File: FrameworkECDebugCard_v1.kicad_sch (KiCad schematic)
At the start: 25 parts, among them J1 Conn_01x05, P1 USB_C_Plug_USB2.0, P2 USB_B_Micro, U1 FT230XS

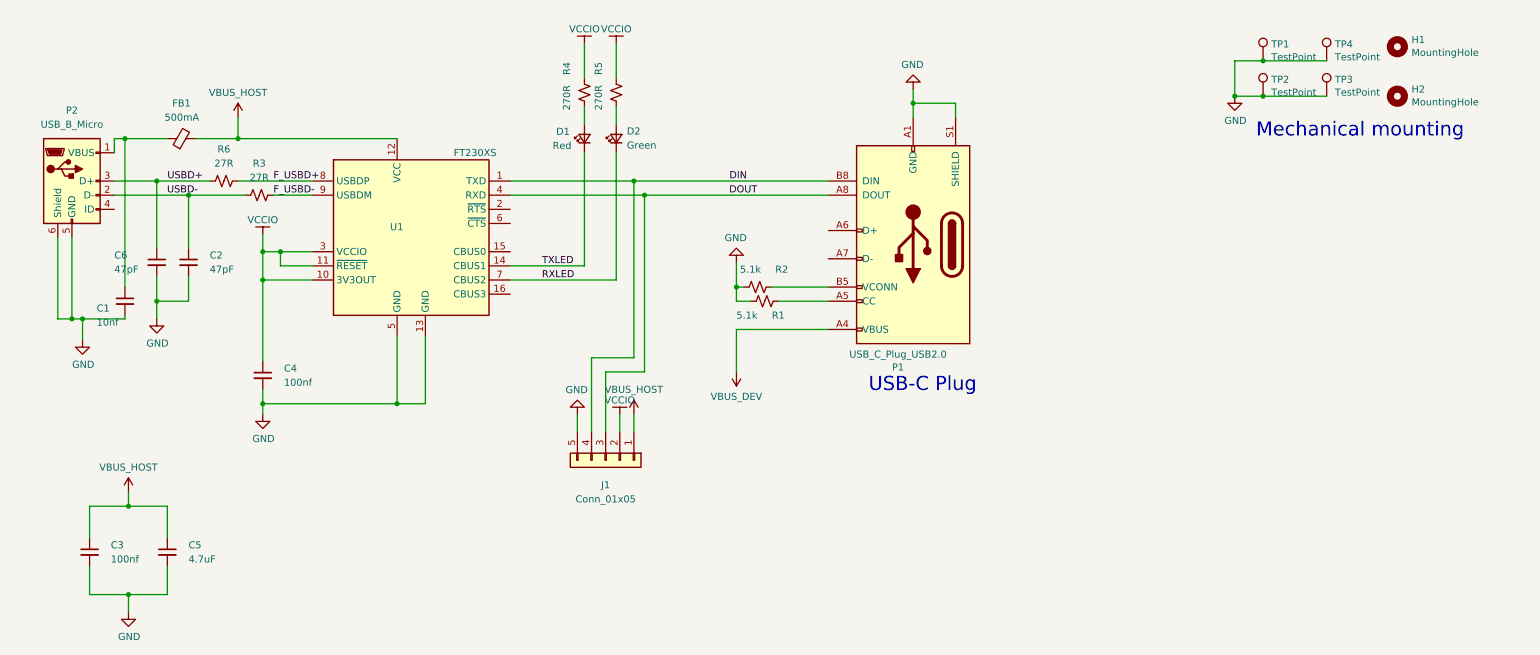
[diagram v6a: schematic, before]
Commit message: ec card 3: recessed mid-mount usb c receptacle, fully rerouted
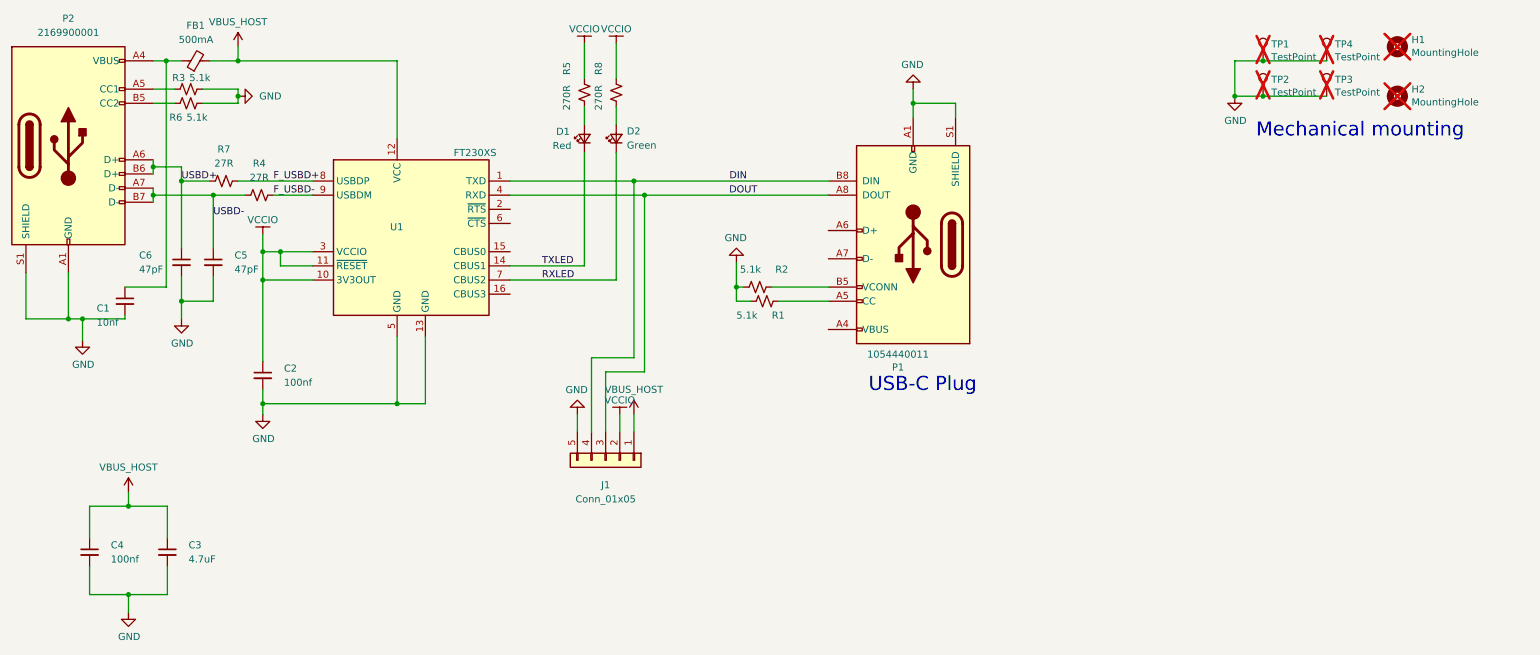
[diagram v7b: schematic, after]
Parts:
- added R3, R6: 5.1k, Resistor_SMD:R_0402_1005Metric, symbol Device:R_Small_US
- H1, H2, TP1, TP2, TP3, TP4: now not fitted
- P1: value USB_C_Plug_USB2.0 -> 1054440011; footprint FrameworkECDebugCard_v1:USB_C_Plug_Molex_105444 -> FrameworkECDebugCard_v1:USB_C_Plug_Molex_105444_SmallPads
- P2: value USB_B_Micro -> 2169900001; footprint Connector_USB:USB_Micro-B_Amphenol_10104110_Horizontal -> FrameworkECDebugCard_v1:USB4510-03-1-A_GCT; symbol Connector:USB_B_Micro -> Connector:USB_C_Receptacle_USB2.0_14P
- renumbered C4 to C2, C5 to C3, C3 to C4, C2 to C5, R3 to R4, R4 to R5, R6 to R7, R5 to R8
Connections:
- net GND: now also P2.A1 (GND), P2.A12 (GND), P2.B1 (GND), P2.B12 (GND), P2.S1 (SHIELD), R3.1, R6.1; no longer P2.5 (GND), P2.6 (Shield)
- net USBD+: now also P2.A6 (D+), P2.B6 (D+); no longer P2.3 (D+)
- net USBD-: now also P2.A7 (D-), P2.B7 (D-); no longer P2.2 (D-)
- net at C1.1, FB1.1: now also P2.A4 (VBUS), P2.A9 (VBUS), P2.B4 (VBUS), P2.B9 (VBUS); no longer P2.1 (VBUS)
- net VBUS_DEV: no longer names the net of P1.A4 (VBUS), P1.A9 (VBUS), P1.B4 (VBUS), P1.B9 (VBUS)
- new net: P2.B5 (CC2), R6.2
- new net: P2.A5 (CC1), R3.2
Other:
- moved on the sheet: C5, C6, FB1

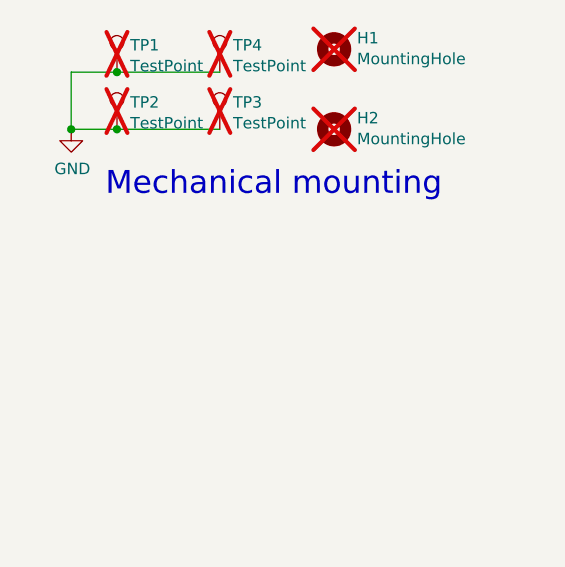
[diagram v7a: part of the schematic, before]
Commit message: ec3: rebuild the pcb to the same shape as the usb c card; not routed
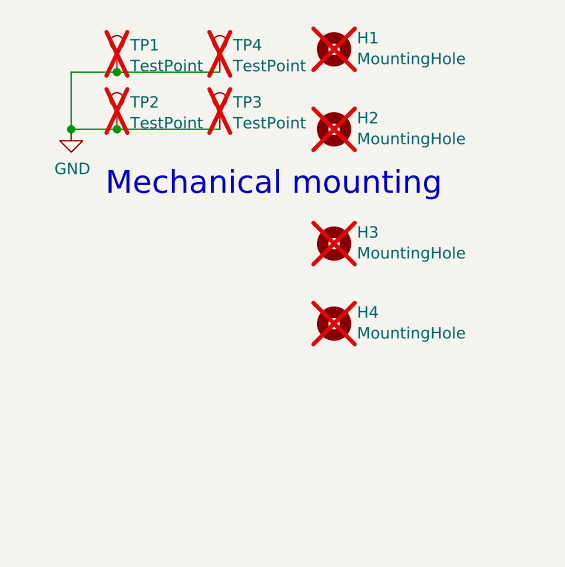
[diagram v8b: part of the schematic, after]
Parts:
- added H3, H4: MountingHole, FrameworkECDebugCard_v1:MountingHole_1.5mm_NPTH, symbol Mechanical:MountingHole
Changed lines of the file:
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@@
+	)
+	(symbol
+		(lib_id "Mechanical:MountingHole")
+		(at 262.89 41.91 0)
+		(unit 1)
+		(exclude_from_sim no)
+		(in_bom yes)
+		(on_board yes)
+		(dnp yes)
+		(property "Reference" "H3"
+			(at 265.43 40.6654 0)
+			(effects
+				(font
+					(size 1.27 1.27)
+				)
+				(justify left)
+			)
+		)
+		(property "Value" "MountingHole"
+			(at 265.43 42.9768 0)
+			(effects
+				(font
+					(size 1.27 1.27)
+				)
+				(justify left)
+			)
+		)
+		(property "Footprint" "FrameworkECDebugCard_v1:MountingHole_1.5mm_NPTH"
+			(at 262.89 41.91 0)
+			(effects
+				(font
+					(size 1.27 1.27)
+				)
+				(hide yes)
+			)
+		)
+		(property "Datasheet" "~"
+			(at 262.89 41.91 0)
+			(effects
+				(font
+					(size 1.27 1.27)
+				)
+				(hide yes)
+			)
+		)
+		(property "Description" ""
+			(at 262.89 41.91 0)
+			(effects
+				(font
+					(size 1.27 1.27)
+				)
+				(hide yes)
+			)
+		)
+		(instances
+			(project "FrameworkECDebugCard_v1"
+				(path "/6d9454a9-630b-4948-a74b-a7b030d302e8"
+					(reference "H3")
+					(unit 1)
+				)
+			)
+		)
 	)
 	(symbol
@@
 					(unit 1)
 				)
+			)
+		)
+	)
+	(symbol
+		(lib_id "Mechanical:MountingHole")
+		(at 262.89 50.8 0)
+		(unit 1)
+		(exclude_from_sim no)
+		(in_bom yes)
+		(on_board yes)
+		(dnp yes)
+		(property "Reference" "H4"
+			(at 265.43 49.5554 0)
+			(effects
+				(font
+					(size 1.27 1.27)
+				)
+				(justify left)
+			)
+		)
+		(property "Value" "MountingHole"
+			(at 265.43 51.8668 0)
+			(effects
+				(font
+					(size 1.27 1.27)
+				)
+				(justify left)
+			)
+		)
+		(property "Footprint" "FrameworkECDebugCard_v1:MountingHole_1.5mm_NPTH"
+			(at 262.89 50.8 0)
+			(effects
+				(font
+					(size 1.27 1.27)
+				)
+				(hide yes)
+			)
+		)
+		(property "Datasheet" "~"
+			(at 262.89 50.8 0)
+			(effects
+				(font
+					(size 1.27 1.27)
+				)
+				(hide yes)
+			)
+		)
+		(property "Description" ""
+			(at 262.89 50.8 0)
+			(effects
+				(font
+					(size 1.27 1.27)
+				)
+				(hide yes)
+			)
+		)
+		(instances
+			(project "FrameworkECDebugCard_v1"
+				(path "/6d9454a9-630b-4948-a74b-a7b030d302e8"
+					(reference "H4")
+					(unit 1)
+				)
